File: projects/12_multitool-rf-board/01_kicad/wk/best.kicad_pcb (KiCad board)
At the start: 4 copper layers, 110 x 46 mm, 87 parts, among them M1 vibro, SW1 RFswitch, SW2 RFswitch, U1 STM32WB55RG, U10 ESD, U2 CC1101, U3 ST25R3916, U5 ST7565R, U6 BQ25896, U7 BQ27220, U8 LM3281, U8B LM3281, U9 loadsw, X10 BAT+NTC, X6 FFC 18p, Y1 32MHz, Y2 32.768kHz

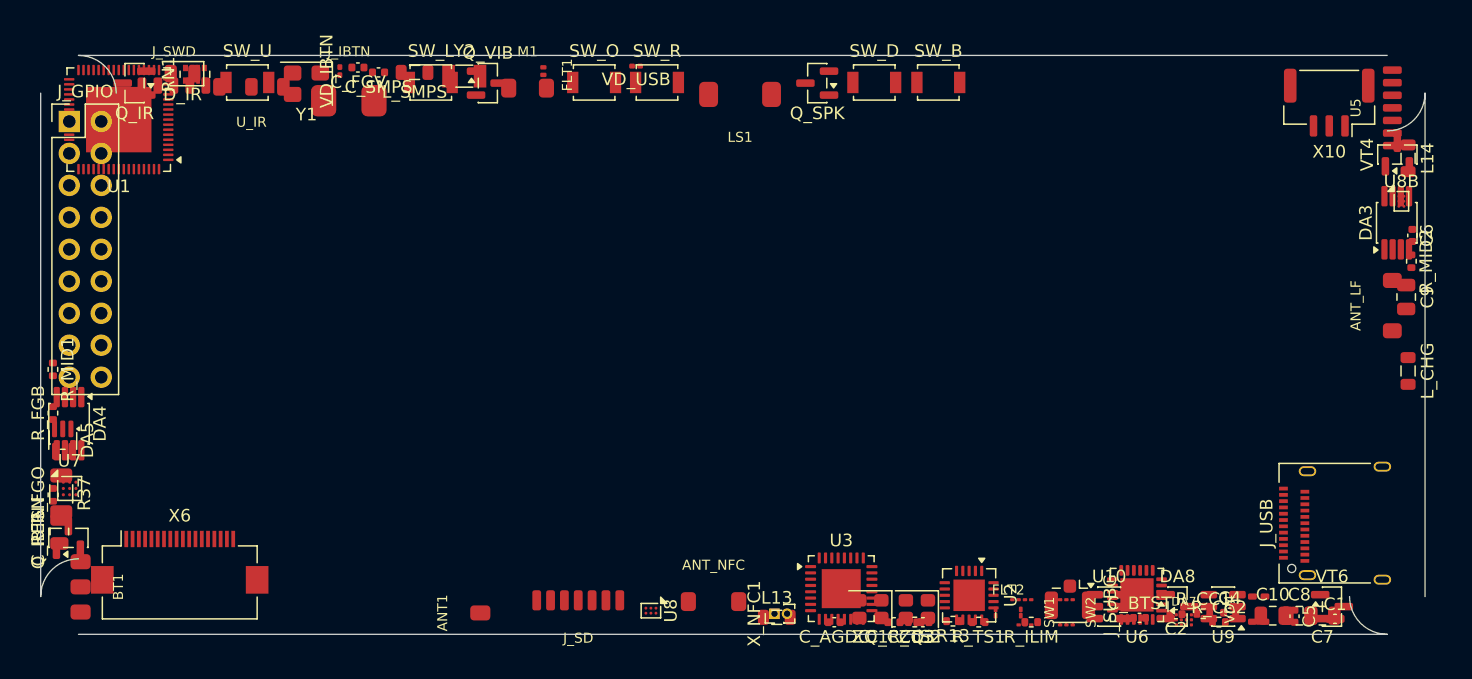
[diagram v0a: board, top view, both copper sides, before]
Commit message: proj12: lock connectors/antennas/buttons on board edges for placement
make_pcb.py: 15 edge parts (USB-C, FFC, GPIO header, SWD, battery, U.FL,
3 antennas, 6 buttons) placed on the outline perimeter and KiCad-locked;
unlocked parts piled below the board as the placer's from-scratch start.
This gives the KiCadRoutingTools placer real edge anchors to organize the
functional groups around (the first unanchored run couldn't converge).

Co-Authored-By: Claude Opus 4.8 <noreply@anthropic.com>
Claude-Session: https://claude.ai/code/session_01Hk6s8R6up8HYVQWXd3atVk
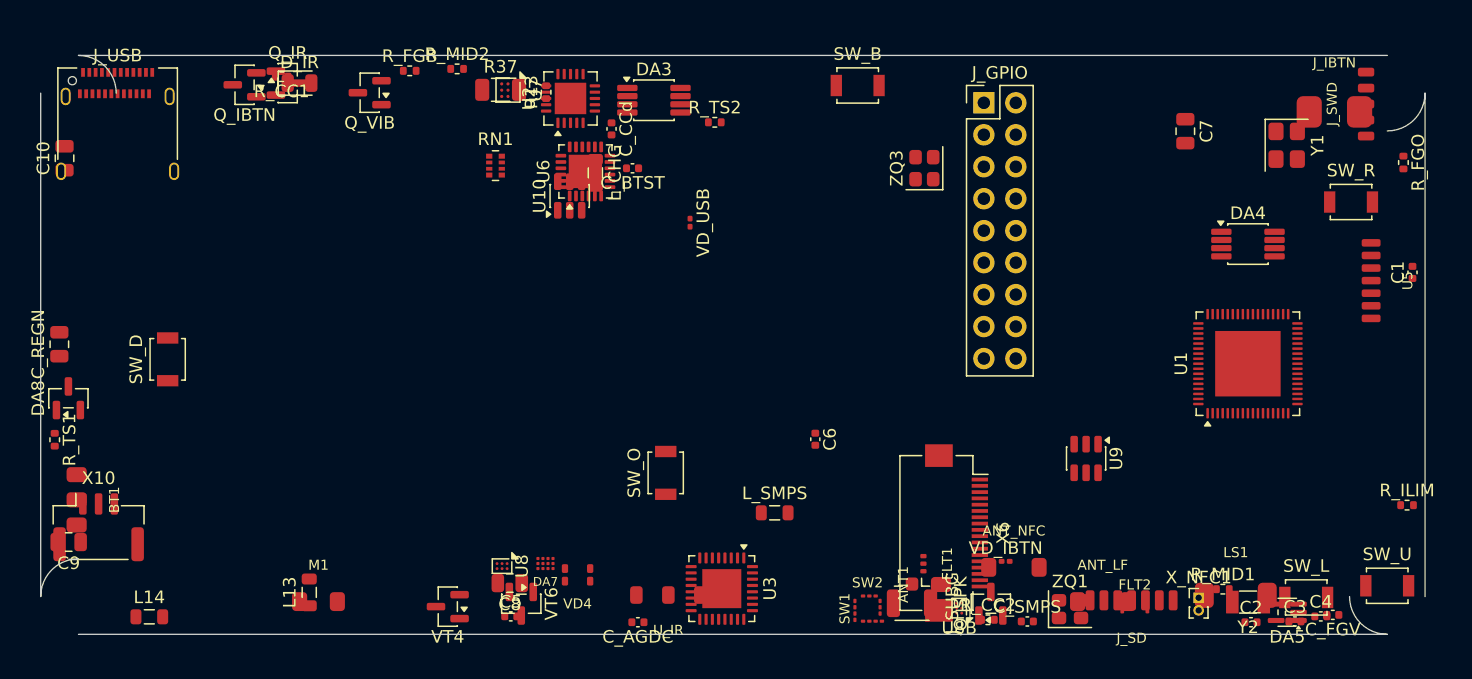
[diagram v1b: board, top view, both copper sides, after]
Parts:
- moved R_FGO 110.5 mm to (138.3, 38.5), turned to 270 degrees
- moved C9 108.0 mm to (32.2, 68.7), turned to 180 degrees
- moved L14 106.4 mm to (38.6, 74.6), turned to 0 degrees
- moved X10 103.4 mm to (34.6, 67.5), turned to 0 degrees
- moved C10 102.7 mm to (31.9, 38.2), turned to 90 degrees
- moved J_USB 102.4 mm to (36.1, 36.4), turned to 0 degrees
- moved SW_U 99.0 mm to (137.0, 72.1)
- moved DA5 98.3 mm to (129.1, 74.2), turned to 180 degrees
- moved DA4 94.8 mm to (125.9, 45.0), turned to 0 degrees
- moved J_SWD 94.7 mm to (135.3, 33.9), turned to 90 degrees
- moved R_MID1 94.6 mm to (123.9, 72.4), turned to 0 degrees
- moved U1 91.8 mm to (125.9, 54.5), turned to 90 degrees
- moved DA8 89.7 mm to (32.2, 57.2), turned to 90 degrees
- moved C_FGV 88.8 mm to (132.7, 74.5)
- moved R_CC1 84.8 mm to (49.1, 31.7), turned to 180 degrees
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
